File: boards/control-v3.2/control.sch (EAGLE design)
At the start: 112 parts, among them IC1 MCP23017-E/SS, J1 2-PIN-KICKERS, J3 HFW8R-1ST, J4 4-PIN-HEADER, J6 DF22-2, Q1 BSS806NH6327XTSA1, Q2 BSS806NH6327XTSA1, U1 XC3S250E-4TQG144C, U11 MCP1824T-1202E/OT, U12 MCP1824T-2502E/OT, U13 TLV70233DBVR, U4 ICM-42605, U5 SN74AHC1G125, U7 MPM3620GQV-P, U8 VND5E006ASPTR-E, X1 ASV-18.432MHZ-EJ-T

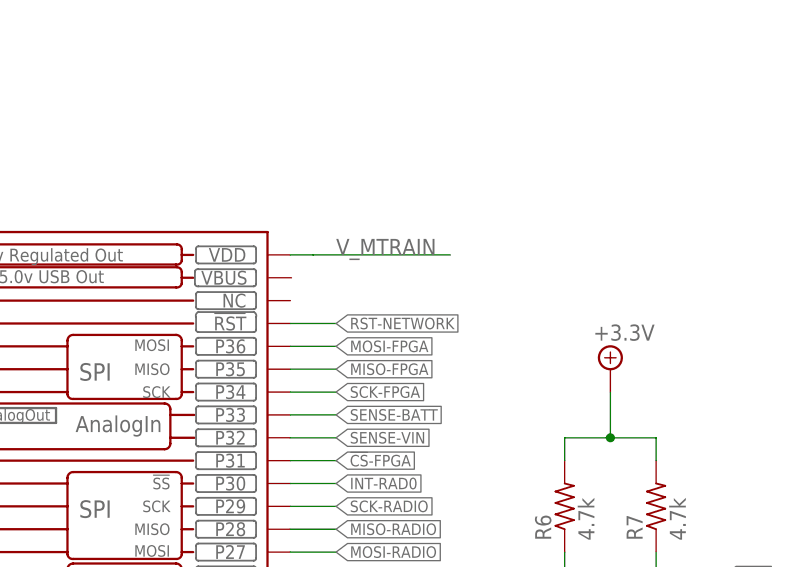
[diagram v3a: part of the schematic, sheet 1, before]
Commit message: Fixed labeling of reset network wires, added via for 1.2V, fixed silkscreen overlap
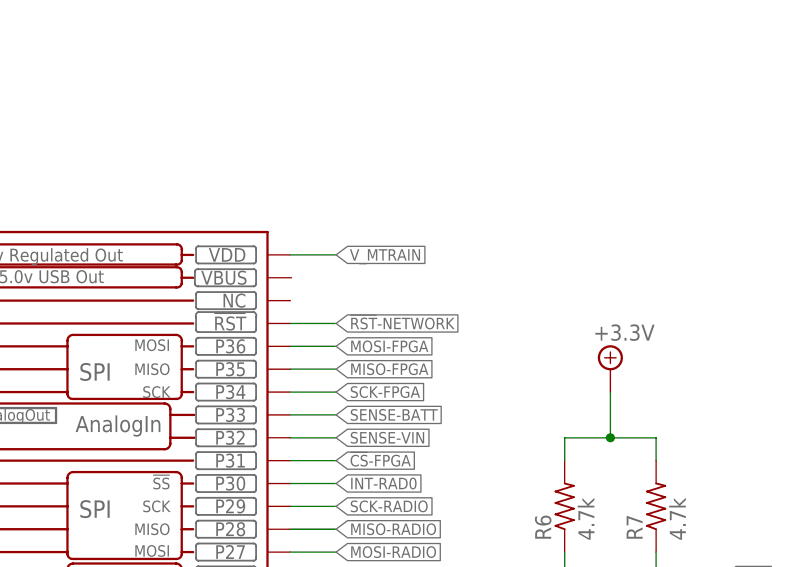
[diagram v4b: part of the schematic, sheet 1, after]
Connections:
- net N$1 renamed BATT_PWR_AVAIL
- net N$3 renamed !RST!_CTRL
- net RST-NETWORK renamed !RST!-NETWORK
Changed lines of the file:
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@@
 <drawing>
 <settings>
-<setting alwaysvectorfont="no"/>
+<setting alwaysvectorfont="yes"/>
 <setting keepoldvectorfont="yes"/>
 <setting verticaltext="up"/>
@@
 <net name="V_MTRAIN" class="0">
 <segment>
-<wire x1="187.96" y1="170.18" x2="190.5" y2="170.18" width="0.1524" layer="91"/>
-<wire x1="190.5" y1="170.18" x2="205.74" y2="170.18" width="0.1524" layer="91"/>
+<wire x1="187.96" y1="170.18" x2="193.04" y2="170.18" width="0.1524" layer="91"/>
 <pinref part="KIT1" gate="G$1" pin="VDD"/>
-<label x="193.04" y="170.18" size="1.778" layer="95"/>
+<label x="193.04" y="170.18" size="1.27" layer="95" xref="yes"/>
 </segment>
 </net>
-<net name="RST-NETWORK" class="0">
+<net name="!RST!-NETWORK" class="0">
 <segment>
 <pinref part="KIT1" gate="G$1" pin="!RST"/>
@@
 </segment>
 </net>
-<net name="N$1" class="0">
+<net name="BATT_PWR_AVAIL" class="0">
 <segment>
 <pinref part="R34" gate="G$1" pin="2"/>
@@
 </segment>
 </net>
-<net name="RST-NETWORK" class="0">
+<net name="!RST!-NETWORK" class="0">
 <segment>
 <wire x1="93.98" y1="185.42" x2="96.52" y2="185.42" width="0.1524" layer="91"/>
@@
 </segment>
 </net>
-<net name="N$3" class="0">
+<net name="!RST!_CTRL" class="0">
 <segment>
 <pinref part="R35" gate="G$1" pin="1"/>

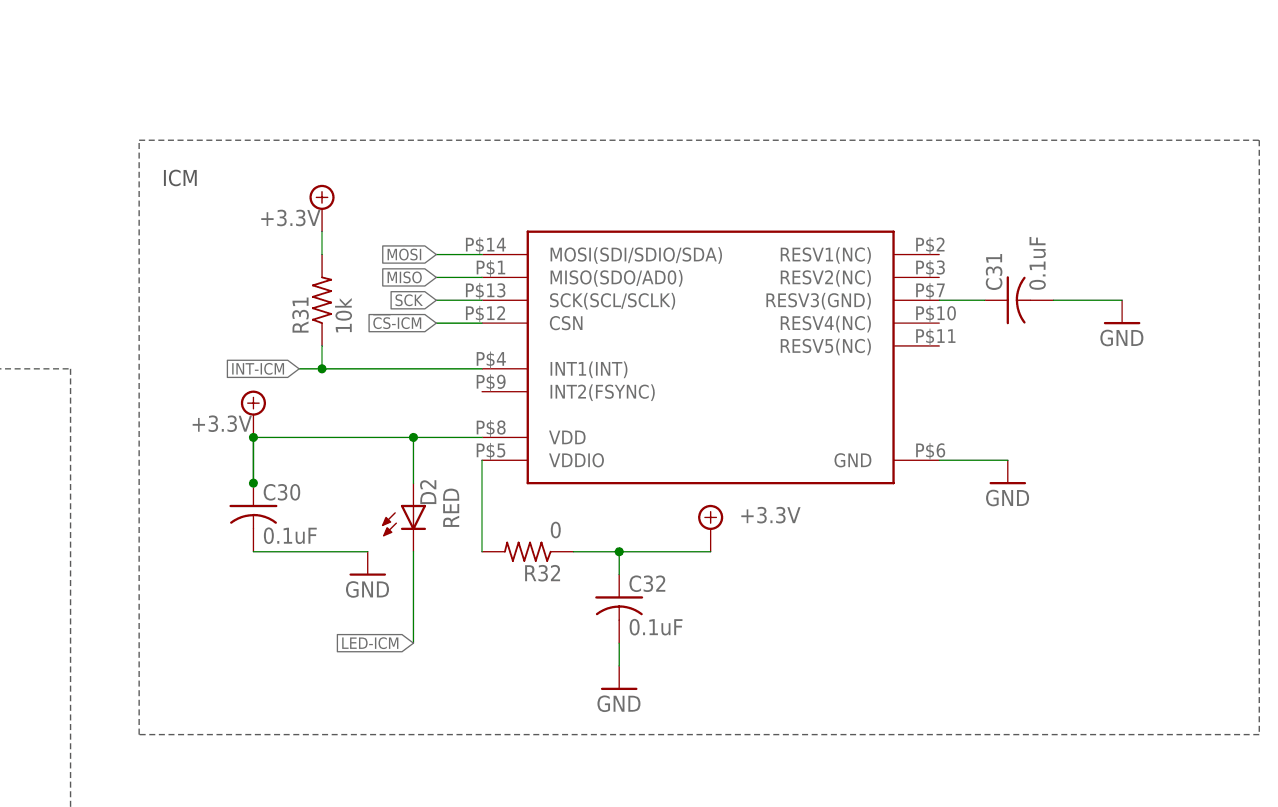
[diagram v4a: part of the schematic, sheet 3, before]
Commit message: Fixed schematic for IMU
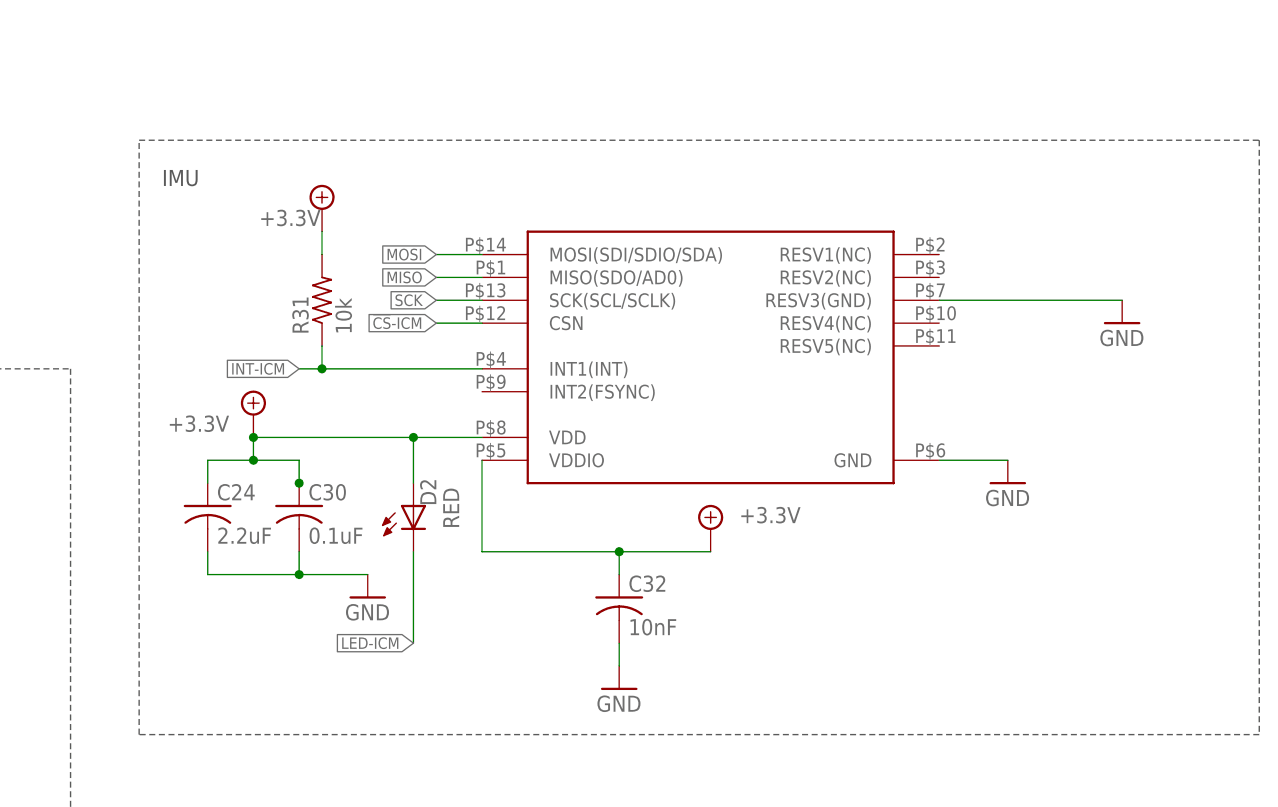
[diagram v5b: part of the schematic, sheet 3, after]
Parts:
- removed C31: 0.1uF, rcl:C-USC0603
- removed R32: 0, resistor:R-US_R0603
- added C24: 2.2uF, rcl:C-USC0603
- C32: value 0.1uF -> 10nF
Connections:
- removed net RESV3: C31.1, U4.RESV3(GND)
- removed net VDDIO: R32.2, U4.VDDIO
- net +3.3V: now also C24.1, U4.VDDIO; no longer R32.1
- net GND: now also C24.2, U4.RESV3(GND); no longer C31.2
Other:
- note added: "IMU"
- note removed: "ICM"
- moved on the sheet: C30
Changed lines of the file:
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@@
 <part name="C30" library="rcl" library_urn="urn:adsk.eagle:library:334" deviceset="C-US" device="C0603" package3d_urn="urn:adsk.eagle:package:23616/2" value="0.1uF"/>
 <part name="GND46" library="supply1" deviceset="GND" device=""/>
-<part name="C31" library="rcl" library_urn="urn:adsk.eagle:library:334" deviceset="C-US" device="C0603" package3d_urn="urn:adsk.eagle:package:23616/2" value="0.1uF"/>
 <part name="GND47" library="supply1" deviceset="GND" device=""/>
 <part name="R31" library="resistor" library_urn="urn:adsk.eagle:library:348" deviceset="R-US_" device="R0603" package3d_urn="urn:adsk.eagle:package:23555/2" value="10k"/>
-<part name="R32" library="resistor" library_urn="urn:adsk.eagle:library:348" deviceset="R-US_" device="R0603" package3d_urn="urn:adsk.eagle:package:23555/2" value="0"/>
-<part name="C32" library="rcl" library_urn="urn:adsk.eagle:library:334" deviceset="C-US" device="C0603" package3d_urn="urn:adsk.eagle:package:23616/2" value="0.1uF"/>
+<part name="C32" library="rcl" library_urn="urn:adsk.eagle:library:334" deviceset="C-US" device="C0603" package3d_urn="urn:adsk.eagle:package:23616/2" value="10nF"/>
 <part name="GND52" library="supply1" deviceset="GND" device=""/>
 <part name="SUPPLY31" library="RoboJackets-Supplies" deviceset="+3.3V" device=""/>
@@
 <part name="Q1" library="RoboJackets-Discrete" deviceset="NMOS" device="SOT-23-3" value="BSS806NH6327XTSA1"/>
 <part name="Q2" library="RoboJackets-Discrete" deviceset="NMOS" device="SOT-23-3" value="BSS806NH6327XTSA1"/>
+<part name="C24" library="rcl" library_urn="urn:adsk.eagle:library:334" deviceset="C-US" device="C0603" package3d_urn="urn:adsk.eagle:package:23616/2" value="2.2uF"/>
 </parts>
 <sheets>
@@
 <wire x1="271.78" y1="48.26" x2="147.32" y2="48.26" width="0.1524" layer="97" style="shortdash"/>
 <wire x1="147.32" y1="48.26" x2="147.32" y2="114.3" width="0.1524" layer="97" style="shortdash"/>
-<text x="149.86" y="109.22" size="1.778" layer="97">ICM</text>
+<text x="149.86" y="109.22" size="1.778" layer="97">IMU</text>
 <wire x1="7.62" y1="88.9" x2="139.7" y2="88.9" width="0.1524" layer="97" style="shortdash"/>
 <wire x1="139.7" y1="88.9" x2="139.7" y2="5.08" width="0.1524" layer="97" style="shortdash"/>
@@
 </instance>
 <instance part="SUPPLY29" gate="P" x="160.02" y="83.82" smashed="yes">
-<attribute name="VALUE" x="153.035" y="81.915" size="1.778" layer="96"/>
-</instance>
-<instance part="C30" gate="G$1" x="160.02" y="73.66" smashed="yes">
-<attribute name="NAME" x="161.036" y="74.295" size="1.778" layer="95"/>
-<attribute name="VALUE" x="161.036" y="69.469" size="1.778" layer="96"/>
-</instance>
-<instance part="GND46" gate="1" x="172.72" y="66.04" smashed="yes">
-<attribute name="VALUE" x="170.18" y="63.5" size="1.778" layer="96"/>
-</instance>
-<instance part="C31" gate="G$1" x="243.84" y="96.52" smashed="yes" rot="R90">
-<attribute name="NAME" x="243.205" y="97.536" size="1.778" layer="95" rot="R90"/>
-<attribute name="VALUE" x="248.031" y="97.536" size="1.778" layer="96" rot="R90"/>
+<attribute name="VALUE" x="150.495" y="81.915" size="1.778" layer="96"/>
+</instance>
+<instance part="C30" gate="G$1" x="165.1" y="73.66" smashed="yes">
+<attribute name="NAME" x="166.116" y="74.295" size="1.778" layer="95"/>
+<attribute name="VALUE" x="166.116" y="69.469" size="1.778" layer="96"/>
+</instance>
+<instance part="GND46" gate="1" x="172.72" y="63.5" smashed="yes">
+<attribute name="VALUE" x="170.18" y="60.96" size="1.778" layer="96"/>
 </instance>
 <instance part="GND47" gate="1" x="256.54" y="93.98" smashed="yes">
@@
 <attribute name="VALUE" x="170.942" y="92.71" size="1.778" layer="96" rot="R90"/>
 </instance>
-<instance part="R32" gate="G$1" x="190.5" y="68.58" smashed="yes" rot="R180">
-<attribute name="NAME" x="194.31" y="67.0814" size="1.778" layer="95" rot="R180"/>
-<attribute name="VALUE" x="194.31" y="71.882" size="1.778" layer="96" rot="R180"/>
-</instance>
 <instance part="C32" gate="G$1" x="200.66" y="63.5" smashed="yes">
 <attribute name="NAME" x="201.676" y="64.135" size="1.778" layer="95"/>
@@
 <attribute name="VALUE" x="96.52" y="162.56" size="1.778" layer="96"/>
 <attribute name="NAME" x="96.52" y="165.1" size="1.778" layer="95"/>
+</instance>
+<instance part="C24" gate="G$1" x="154.94" y="73.66" smashed="yes">
+<attribute name="NAME" x="155.956" y="74.295" size="1.778" layer="95"/>
+<attribute name="VALUE" x="155.956" y="69.469" size="1.778" layer="96"/>
 </instance>
 </instances>
@@
 </segment>
 <segment>
-<pinref part="GND46" gate="1" pin="GND"/>
-<pinref part="C30" gate="G$1" pin="2"/>
-<wire x1="172.72" y1="68.58" x2="160.02" y2="68.58" width="0.1524" layer="91"/>
-</segment>
-<segment>
-<pinref part="C31" gate="G$1" pin="2"/>
 <pinref part="GND47" gate="1" pin="GND"/>
-<wire x1="248.92" y1="96.52" x2="256.54" y2="96.52" width="0.1524" layer="91"/>
+<pinref part="U4" gate="G$1" pin="RESV3(GND)"/>
+<wire x1="236.22" y1="96.52" x2="256.54" y2="96.52" width="0.1524" layer="91"/>
 </segment>
 <segment>
@@
 <wire x1="93.98" y1="157.48" x2="93.98" y2="144.78" width="0.1524" layer="91"/>
 <pinref part="Q2" gate="G$1" pin="S"/>
+</segment>
+<segment>
+<pinref part="GND46" gate="1" pin="GND"/>
+<pinref part="C24" gate="G$1" pin="2"/>
+<wire x1="154.94" y1="68.58" x2="154.94" y2="66.04" width="0.1524" layer="91"/>
+<wire x1="154.94" y1="66.04" x2="165.1" y2="66.04" width="0.1524" layer="91"/>
+<pinref part="C30" gate="G$1" pin="2"/>
+<wire x1="165.1" y1="66.04" x2="172.72" y2="66.04" width="0.1524" layer="91"/>
+<wire x1="165.1" y1="68.58" x2="165.1" y2="66.04" width="0.1524" layer="91"/>
+<junction x="165.1" y="66.04"/>
 </segment>
 </net>
@@
 <segment>
 <pinref part="SUPPLY29" gate="P" pin="+3.3V"/>
-<wire x1="160.02" y1="81.28" x2="160.02" y2="76.2" width="0.1524" layer="91"/>
-<wire x1="160.02" y1="76.2" x2="160.02" y2="81.28" width="0.1524" layer="91"/>
-<junction x="160.02" y="81.28"/>
 <pinref part="U4" gate="G$1" pin="VDD"/>
 <wire x1="185.42" y1="81.28" x2="177.8" y2="81.28" width="0.1524" layer="91"/>
-<pinref part="C30" gate="G$1" pin="1"/>
-<junction x="160.02" y="76.2"/>
 <pinref part="D2" gate="G$1" pin="A"/>
 <wire x1="177.8" y1="81.28" x2="160.02" y2="81.28" width="0.1524" layer="91"/>
 <wire x1="177.8" y1="76.2" x2="177.8" y2="81.28" width="0.1524" layer="91"/>
 <junction x="177.8" y="81.28"/>
+<pinref part="C24" gate="G$1" pin="1"/>
+<pinref part="C30" gate="G$1" pin="1"/>
+<junction x="165.1" y="76.2"/>
+<wire x1="165.1" y1="76.2" x2="165.1" y2="78.74" width="0.1524" layer="91"/>
+<wire x1="165.1" y1="78.74" x2="160.02" y2="78.74" width="0.1524" layer="91"/>
+<wire x1="160.02" y1="78.74" x2="154.94" y2="78.74" width="0.1524" layer="91"/>
+<wire x1="154.94" y1="78.74" x2="154.94" y2="76.2" width="0.1524" layer="91"/>
+<wire x1="160.02" y1="81.28" x2="160.02" y2="78.74" width="0.1524" layer="91"/>
+<junction x="160.02" y="81.28"/>
+<junction x="160.02" y="78.74"/>
 </segment>
 <segment>
@@
 <pinref part="C32" gate="G$1" pin="1"/>
 <wire x1="200.66" y1="66.04" x2="200.66" y2="68.58" width="0.1524" layer="91"/>
-<pinref part="R32" gate="G$1" pin="1"/>
-<wire x1="200.66" y1="68.58" x2="195.58" y2="68.58" width="0.1524" layer="91"/>
 <pinref part="SUPPLY31" gate="P" pin="+3.3V"/>
 <wire x1="200.66" y1="68.58" x2="210.82" y2="68.58" width="0.1524" layer="91"/>
 <junction x="200.66" y="68.58"/>
+<pinref part="U4" gate="G$1" pin="VDDIO"/>
+<wire x1="185.42" y1="68.58" x2="185.42" y2="78.74" width="0.1524" layer="91"/>
+<wire x1="185.42" y1="68.58" x2="200.66" y2="68.58" width="0.1524" layer="91"/>
 </segment>
 <segment>
@@
 </segment>
 </net>
-<net name="RESV3" class="0">
-<segment>
-<pinref part="U4" gate="G$1" pin="RESV3(GND)"/>
-<pinref part="C31" gate="G$1" pin="1"/>
-<wire x1="236.22" y1="96.52" x2="241.3" y2="96.52" width="0.1524" layer="91"/>
-</segment>
-</net>
-<net name="VDDIO" class="0">
-<segment>
-<pinref part="R32" gate="G$1" pin="2"/>
-<pinref part="U4" gate="G$1" pin="VDDIO"/>
-<wire x1="185.42" y1="68.58" x2="185.42" y2="78.74" width="0.1524" layer="91"/>
-</segment>
-</net>
